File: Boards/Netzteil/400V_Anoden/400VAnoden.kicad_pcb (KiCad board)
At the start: 2 copper layers, 160 x 100 mm, 46 parts, among them P1 Drossel, P2 320V_AC, P3 Stabi, P4 133V_AC, P5 Stabi, P6 Trafo, P7 Trafo, Q1 2SC2979

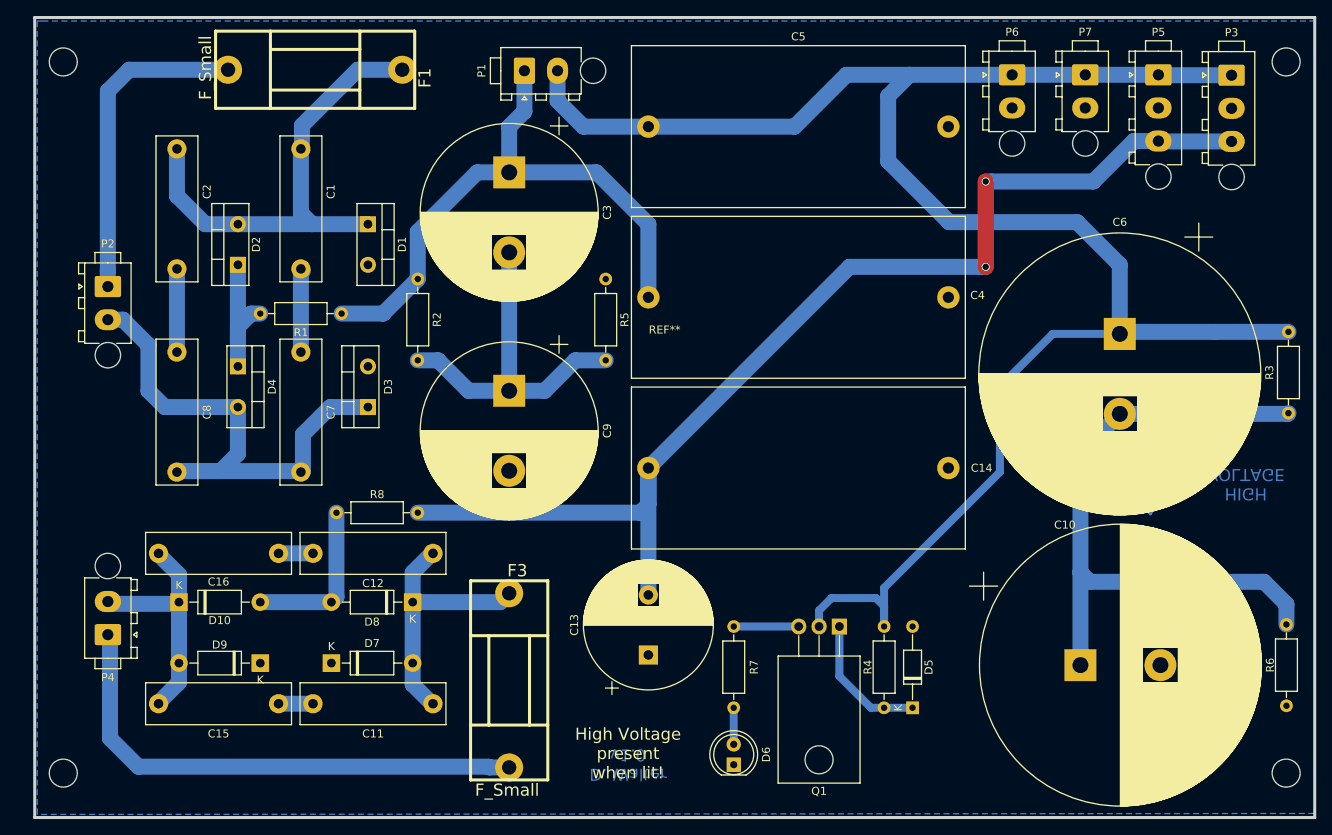
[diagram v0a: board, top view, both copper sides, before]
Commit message: HV Switch on delay added
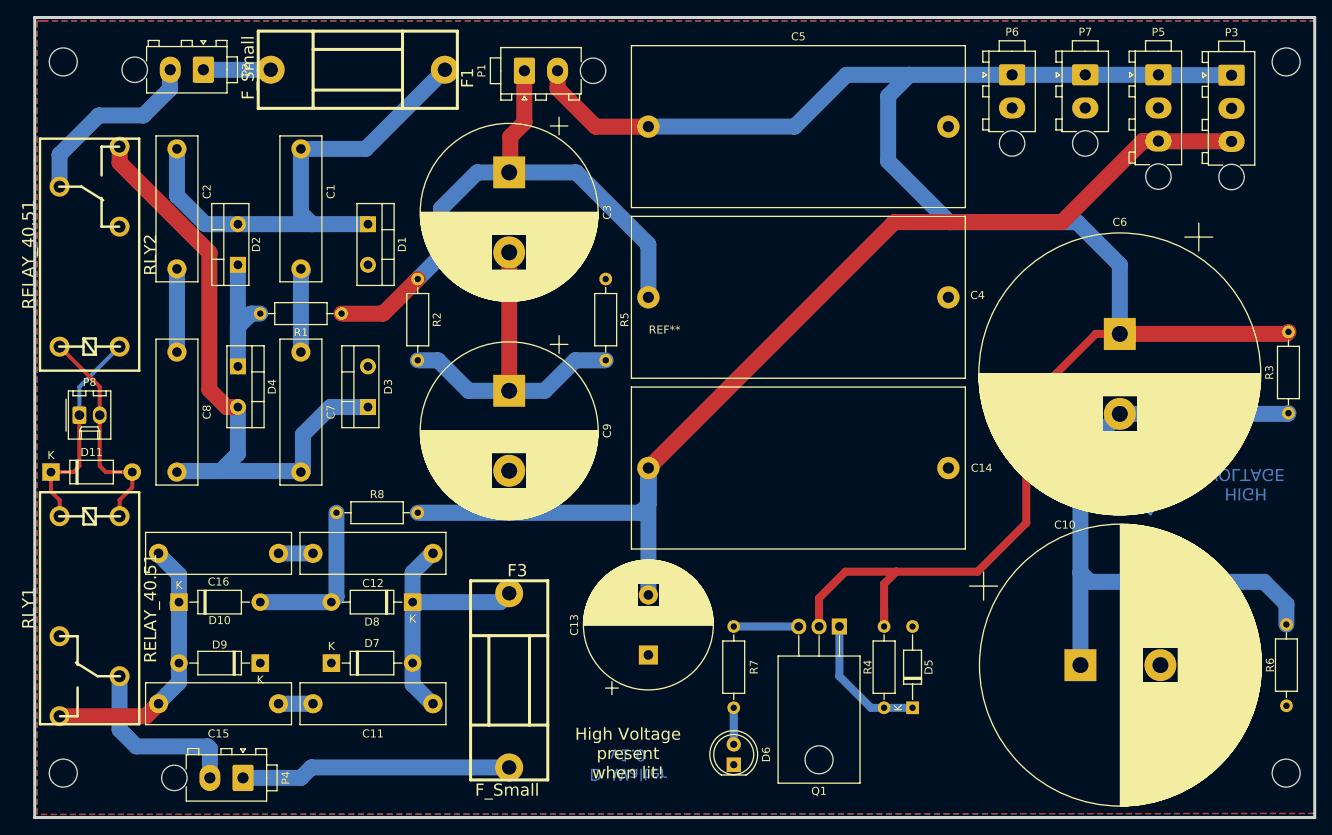
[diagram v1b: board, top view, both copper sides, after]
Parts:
- added D11: 1N4001, Diode_THT:D_DO-41_SOD81_P10.16mm_Horizontal, F.Cu at (38.6, 83.8)
- added P8: Relay, Connector_Molex:Molex_KK-254_AE-6410-02A_1x02_P2.54mm_Vertical, F.Cu at (42.2, 76.7)
- added RLY1: RELAY_40.51, w_relay:relay_40.51, F.Cu at (43.4, 100.8)
- added RLY2: RELAY_40.51, w_relay:relay_40.51, F.Cu at (43.4, 56.6)
- moved P2 29.6 mm to (57.7, 33.5), turned to 270 degrees
- moved P4 24.6 mm to (62.6, 122.0), turned to 270 degrees
- moved F1 5.33 mm to (77.0, 33.5)
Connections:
- P2 pad 2: Net-(C7-Pad2) -> Net-(P2-Pad2)
- P4 pad 2: Net-(C15-Pad2) -> Net-(P4-Pad2)
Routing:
- net Net-(F1-Pad1): track 40.4 -> 8.42 mm
- net Net-(F3-Pad1): track 64.1 -> 33.8 mm
- net Net-(D11-Pad2): track 0.00 -> 27.5 mm
- net Net-(D11-Pad1): track 0.00 -> 26.8 mm
- net Net-(P2-Pad2): track 0.00 -> 23.6 mm
- net Net-(P4-Pad2): track 0.00 -> 22.6 mm
- net Net-(C7-Pad2): track 68.6 -> 83.7 mm
- net /+450V_DC: track 234.6 -> 240.0 mm
- net /-180V_DC: track 144.9 -> 139.5 mm, vias 2 -> 0
- net Net-(C15-Pad2): track 29.7 -> 34.3 mm
- net Net-(C1-Pad1): track 59.7 -> 63.3 mm
- net Net-(C3-Pad1): track 74.3 -> 73.0 mm
- added copper zone on F.Cu, net GND

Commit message: Added Vias & Mounting Holes
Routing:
- net GND: vias 0 -> 32
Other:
- board text removed: "Bot"
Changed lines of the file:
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@@
   (general
     (thickness 1.6)
-    (drawings 4)
-    (tracks 159)
+    (drawings 3)
+    (tracks 191)
     (zones 0)
     (modules 50)
@@
     (47 F.CrtYd user)
     (48 B.Fab user)
-    (49 F.Fab user)
+    (49 F.Fab user hide)
   )
   (setup
-    (last_trace_width 1)
+    (last_trace_width 0.5)
     (user_trace_width 0.5)
     (user_trace_width 1)
@@
     (pad_to_mask_clearance 0.2)
     (aux_axis_origin 0 0)
-    (visible_elements 7FFFFFFF)
+    (visible_elements 7FFDFF7F)
     (pcbplotparams
       (layerselection 0x00030_80000001)
@@
     (at 43.434 56.642 90)
     (descr "relay, 40.51")
-    (fp_text reference RLY2 (at 0 7.62 90) (layer F.SilkS)
+    (fp_text reference RLY2 (at -7.112 7.874 90) (layer F.SilkS)
       (effects (font (size 1.524 1.524) (thickness 0.3048)))
     )
-    (fp_text value RELAY_40.51 (at 0 -7.62 90) (layer F.SilkS)
+    (fp_text value RELAY_40.51 (at 0 -7.62 90) (layer F.SilkS) hide
       (effects (font (size 1.524 1.524) (thickness 0.3048)))
     )
@@
     (at 43.434 100.838 270)
     (descr "relay, 40.51")
-    (fp_text reference RLY1 (at 0 7.62 90) (layer F.SilkS)
+    (fp_text reference RLY1 (at 0 -7.62 90) (layer F.SilkS)
       (effects (font (size 1.524 1.524) (thickness 0.3048)))
     )
-    (fp_text value RELAY_40.51 (at 0 -7.62 90) (layer F.SilkS)
+    (fp_text value RELAY_40.51 (at 0 -7.62 90) (layer F.SilkS) hide
       (effects (font (size 1.524 1.524) (thickness 0.3048)))
     )
@@
     (tags "Symbol, High Voltage, Type 2, Copper Top, Very Small,")
     (attr virtual)
-    (fp_text reference REF** (at -0.127 5.715) (layer B.SilkS)
+    (fp_text reference REF** (at -0.127 5.715) (layer B.SilkS) hide
       (effects (font (size 1 1) (thickness 0.15)) (justify mirror))
     )
@@
     (descr "Outline, Eurocard, 100x160mm, with holes 3,5mm,")
     (tags "Outline, Eurocard, 100x160mm, with holes 3,5mm,")
-    (fp_text reference REF** (at 78.74 -60.96) (layer F.SilkS)
+    (fp_text reference REF** (at 78.74 -60.96) (layer F.SilkS) hide
       (effects (font (size 1 1) (thickness 0.15)))
     )
@@
       (effects (font (size 1.524 1.524) (thickness 0.3048)))
     )
-    (fp_text value F_Small (at 0.254 -13.716 90) (layer F.SilkS)
+    (fp_text value F_Small (at 0.254 -13.716 90) (layer F.SilkS) hide
       (effects (font (size 1.524 1.524) (thickness 0.3048)))
     )
@@
       (effects (font (size 1.524 1.524) (thickness 0.3048)))
     )
-    (fp_text value F_Small (at 0.254 -13.716 180) (layer F.SilkS)
+    (fp_text value F_Small (at 0.254 -13.716 180) (layer F.SilkS) hide
       (effects (font (size 1.524 1.524) (thickness 0.3048)))
     )
@@
     (effects (font (size 1.5 1.5) (thickness 0.3)) (justify mirror))
   )
-  (gr_text Bot (at 178.562 122.174 180) (layer B.Cu)
-    (effects (font (size 1.5 1.5) (thickness 0.3)) (justify mirror))
-  )
   (segment (start 61.976 52.832) (end 71.247 52.832) (width 2) (layer B.Cu) (net 1) (status 10))
   (segment (start 71.247 52.832) (end 78.232 52.832) (width 2) (layer B.Cu) (net 1) (status 20))
@@
   (segment (start 86.995 69.85) (end 90.805 73.66) (width 2) (layer B.Cu) (net 5))
   (segment (start 95.885 73.66) (end 95.885 56.355) (width 2) (layer F.Cu) (net 5) (status 30))
+  (via (at 123.698 83.312) (size 1) (drill 0.8) (layers F.Cu B.Cu) (net 6))
+  (via (at 141.732 83.312) (size 1) (drill 0.8) (layers F.Cu B.Cu) (net 6))
+  (via (at 141.732 61.976) (size 1) (drill 0.8) (layers F.Cu B.Cu) (net 6))
+  (via (at 123.444 61.976) (size 1) (drill 0.8) (layers F.Cu B.Cu) (net 6))
+  (via (at 123.444 46.482) (size 1) (drill 0.8) (layers F.Cu B.Cu) (net 6))
+  (via (at 123.444 33.782) (size 1) (drill 0.8) (layers F.Cu B.Cu) (net 6))
+  (via (at 158.75 48.26) (size 1) (drill 0.8) (layers F.Cu B.Cu) (net 6))
+  (via (at 158.75 57.15) (size 1) (drill 0.8) (layers F.Cu B.Cu) (net 6))
+  (via (at 64.77 103.632) (size 1) (drill 0.8) (layers F.Cu B.Cu) (net 6))
+  (via (at 73.66 103.378) (size 1) (drill 0.8) (layers F.Cu B.Cu) (net 6))
+  (via (at 69.088 103.632) (size 1) (drill 0.8) (layers F.Cu B.Cu) (net 6))
+  (via (at 69.85 72.898) (size 1) (drill 0.8) (layers F.Cu B.Cu) (net 6))
+  (via (at 69.596 55.118) (size 1) (drill 0.8) (layers F.Cu B.Cu) (net 6))
+  (via (at 54.356 76.2) (size 1) (drill 0.8) (layers F.Cu B.Cu) (net 6))
+  (via (at 61.976 43.434) (size 1) (drill 0.8) (layers F.Cu B.Cu) (net 6))
+  (via (at 43.434 57.912) (size 1) (drill 0.8) (layers F.Cu B.Cu) (net 6))
+  (via (at 43.434 98.806) (size 1) (drill 0.8) (layers F.Cu B.Cu) (net 6))
+  (via (at 142.748 119.634) (size 1) (drill 0.8) (layers F.Cu B.Cu) (net 6))
+  (via (at 103.632 93.726) (size 1) (drill 0.8) (layers F.Cu B.Cu) (net 6))
+  (via (at 91.186 64.008) (size 1) (drill 0.8) (layers F.Cu B.Cu) (net 6))
+  (via (at 101.092 64.008) (size 1) (drill 0.8) (layers F.Cu B.Cu) (net 6))
+  (via (at 39.37 57.912) (size 1) (drill 0.8) (layers F.Cu B.Cu) (net 6))
+  (via (at 47.752 57.912) (size 1) (drill 0.8) (layers F.Cu B.Cu) (net 6))
+  (via (at 39.624 98.806) (size 1) (drill 0.8) (layers F.Cu B.Cu) (net 6))
+  (via (at 47.244 98.806) (size 1) (drill 0.8) (layers F.Cu B.Cu) (net 6))
+  (via (at 83.566 43.434) (size 1) (drill 0.8) (layers F.Cu B.Cu) (net 6))
+  (via (at 131.826 83.312) (size 1) (drill 0.8) (layers F.Cu B.Cu) (net 6))
+  (via (at 59.69 87.122) (size 1) (drill 0.8) (layers F.Cu B.Cu) (net 6))
+  (via (at 77.978 82.55) (size 1) (drill 0.8) (layers F.Cu B.Cu) (net 6))
+  (via (at 139.192 40.894) (size 1) (drill 0.8) (layers F.Cu B.Cu) (net 6))
+  (via (at 95.758 109.474) (size 1) (drill 0.8) (layers F.Cu B.Cu) (net 6))
+  (via (at 153.162 119.634) (size 1) (drill 0.8) (layers F.Cu B.Cu) (net 6))
   (segment (start 172.212 76.548) (end 167.292 81.468) (width 2) (layer B.Cu) (net 7) (status 10))
   (segment (start 193.2 76.548) (end 193.294 76.454) (width 2) (layer B.Cu) (net 7) (status 30))

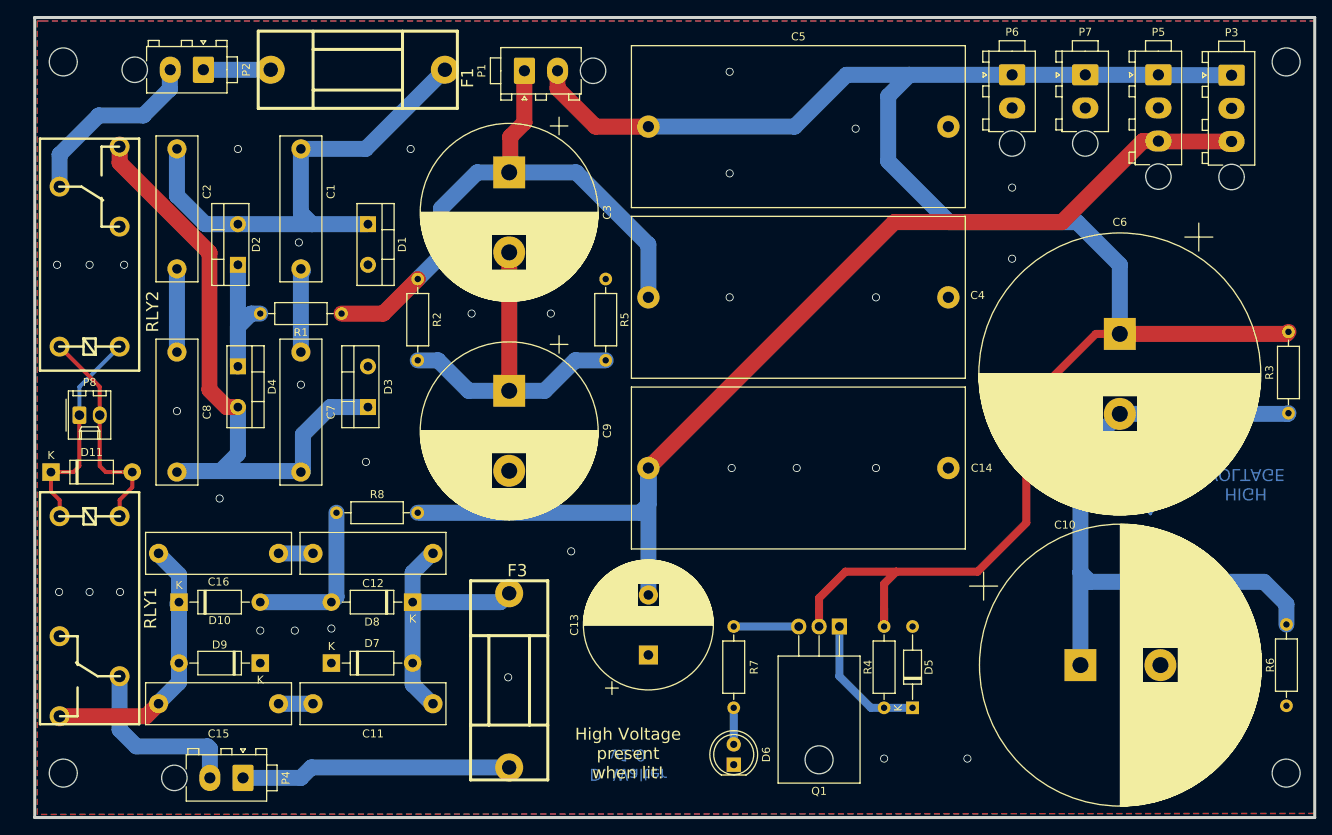
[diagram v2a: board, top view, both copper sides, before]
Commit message: Added Test, moved mounting holes
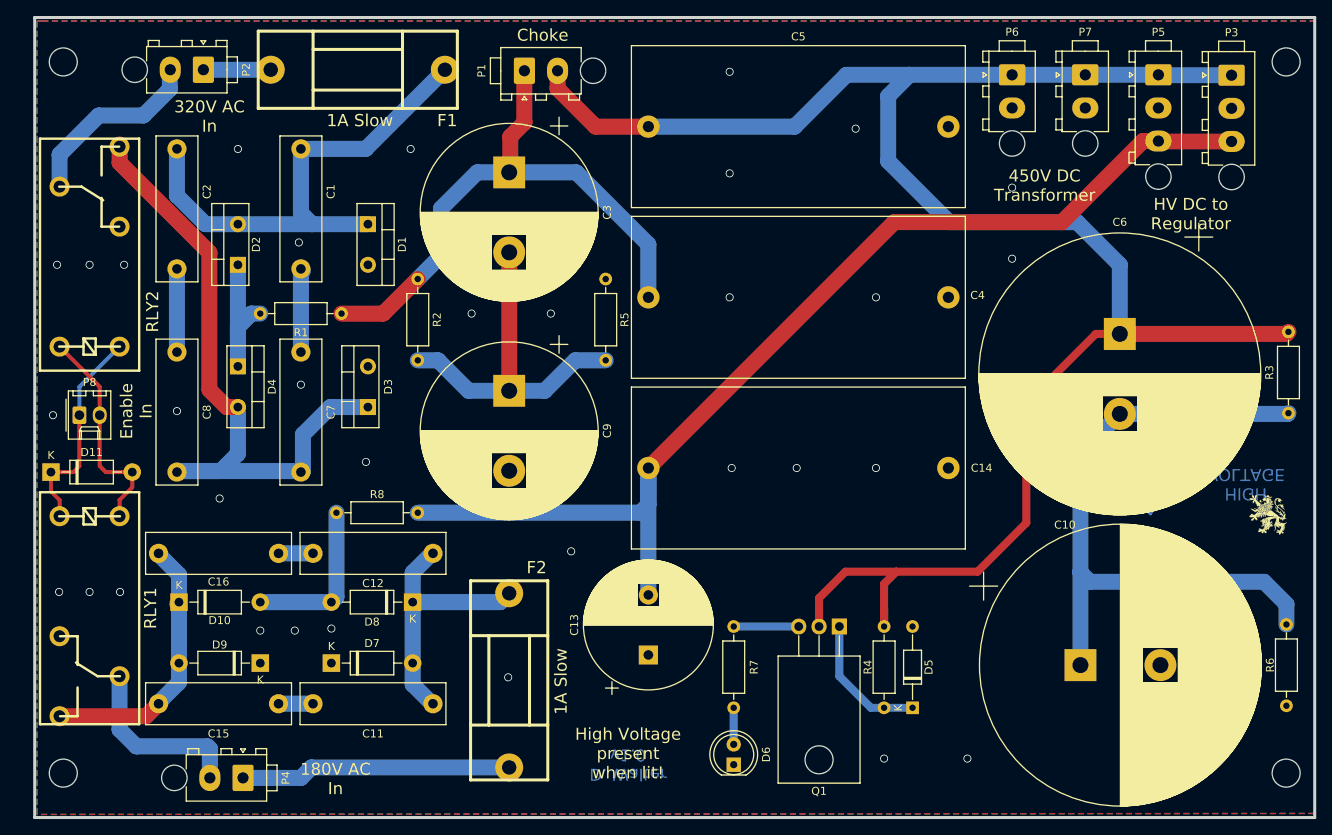
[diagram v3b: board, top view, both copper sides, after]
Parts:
- added G***: LOGO, Loewe:Loewe_Klein, F.Cu at (190.8, 89.2)
- F1: value F_Small -> 1A Slow
- F2: renamed from F3; value F_Small -> 1A Slow
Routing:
- net GND: vias 32 -> 33
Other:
- board text added: "180V AC In"
- board text added: "320V AC In"
- board text added: "450V DC Transformer"
- board text added: "Choke"
- board text added: "Enable In"
- board text added: "HV DC to Regulator"
